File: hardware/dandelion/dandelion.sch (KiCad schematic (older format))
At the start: 102 parts, among them J1 PCB antenna, J2 USB-MICRO-B, P1 DIGITAL, P10 GIO6, P11 DCLK, P12 DIO, P13 PCB JUMPER, P14 E8A, P15 R8C PROGRAM, P16 R8C EXPAND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

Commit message: Dandelion: minor BOM correction
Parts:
- D16: Field4 (none) -> DIY
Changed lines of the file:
@@
-EESchema Schematic File Version 2  date Sat 27 Aug 2011 03:56:37 PM MDT
+EESchema Schematic File Version 2  date Sat 27 Aug 2011 04:10:09 PM MDT
 LIBS:ubertooth-symbols
 LIBS:power
@@
 F 5 "RB521S30" H 3650 9250 60  0001 C CNN "Field2"
 F 6 "DIODE SCHOTTKY 30V 200MA SOD523F" H 3650 9250 60  0001 C CNN "Field3"
+F 7 "DIY" H 3650 9250 60  0001 C CNN "Field4"
 	1    3650 9250
 	0    1    1    0

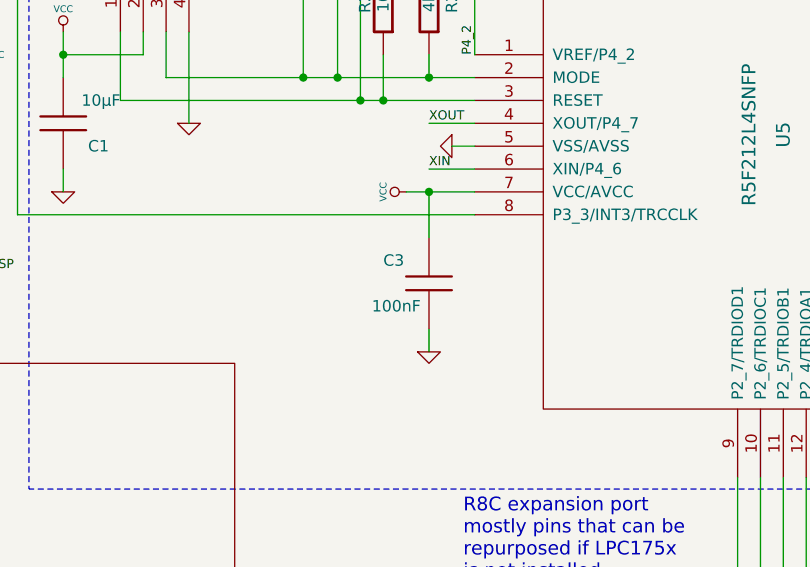
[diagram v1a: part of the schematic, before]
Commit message: Dandelion: another minor BOM correction
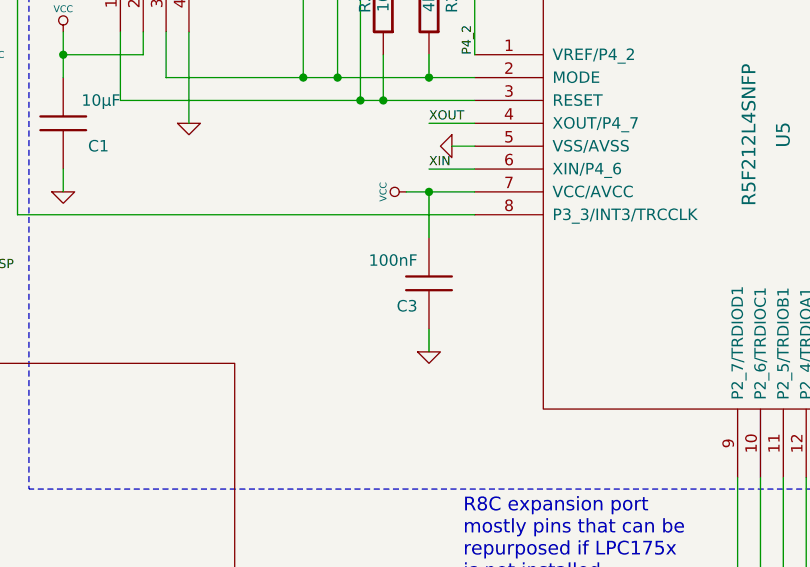
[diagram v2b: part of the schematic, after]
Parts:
- C3: footprint 0603 -> (none); Field1 TDK -> Murata; Field2 C1608X7R1H104K -> GRM155R71C104KA88D; Field3 Multilayer Ceramic Capacitors (MLCC) - SMD/SMT 0603 0.1uF 5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 -> Multilayer Ceramic Capacitors (MLCC) - SMD/SMT 0402 0.1uF 1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
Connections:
- net GND: now also C3.1; no longer C3.2
- net VCC: now also C3.2; no longer C3.1
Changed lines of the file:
@@
-EESchema Schematic File Version 2  date Sat 27 Aug 2011 04:10:09 PM MDT
+EESchema Schematic File Version 2  date Sat 27 Aug 2011 04:22:05 PM MDT
 LIBS:ubertooth-symbols
 LIBS:power
@@
 Comment4 ""
 $EndDescr
+$Comp
+L C C3
+U 1 1 4E596DF5
+P 12600 3100
+F 0 "C3" H 12650 3200 50  0000 L CNN
+F 1 "100nF" H 12650 3000 50  0000 L CNN
+F 4 "Murata" H 12600 3100 60  0001 C CNN "Field1"
+F 5 "GRM155R71C104KA88D" H 12600 3100 60  0001 C CNN "Field2"
+F 6 "Multilayer Ceramic Capacitors (MLCC) - SMD/SMT 0402 0.1uF 16volts X7R 10%" H 12600 3100 60  0001 C CNN "Field3"
+	1    12600 3100
+	-1   0    0    1
+$EndComp
 NoConn ~ 11900 1100
 Connection ~ 12300 2300
@@
 	1    0    0    -1
 $EndComp
-$Comp
-L C C3
-U 1 1 4E583A6B
-P 12600 3100
-F 0 "C3" H 12400 3200 50  0000 L CNN
-F 1 "100nF" H 12350 3000 50  0000 L CNN
-F 2 "0603" H 12600 3100 60  0001 C CNN
-F 4 "TDK" H 12600 3100 60  0001 C CNN "Field1"
-F 5 "C1608X7R1H104K" H 12600 3100 60  0001 C CNN "Field2"
-F 6 "Multilayer Ceramic Capacitors (MLCC) - SMD/SMT 0603 0.1uF 50volts X7R 10%" H 12600 3100 60  0001 C CNN "Field3"
-	1    12600 3100
-	1    0    0    -1
-$EndComp

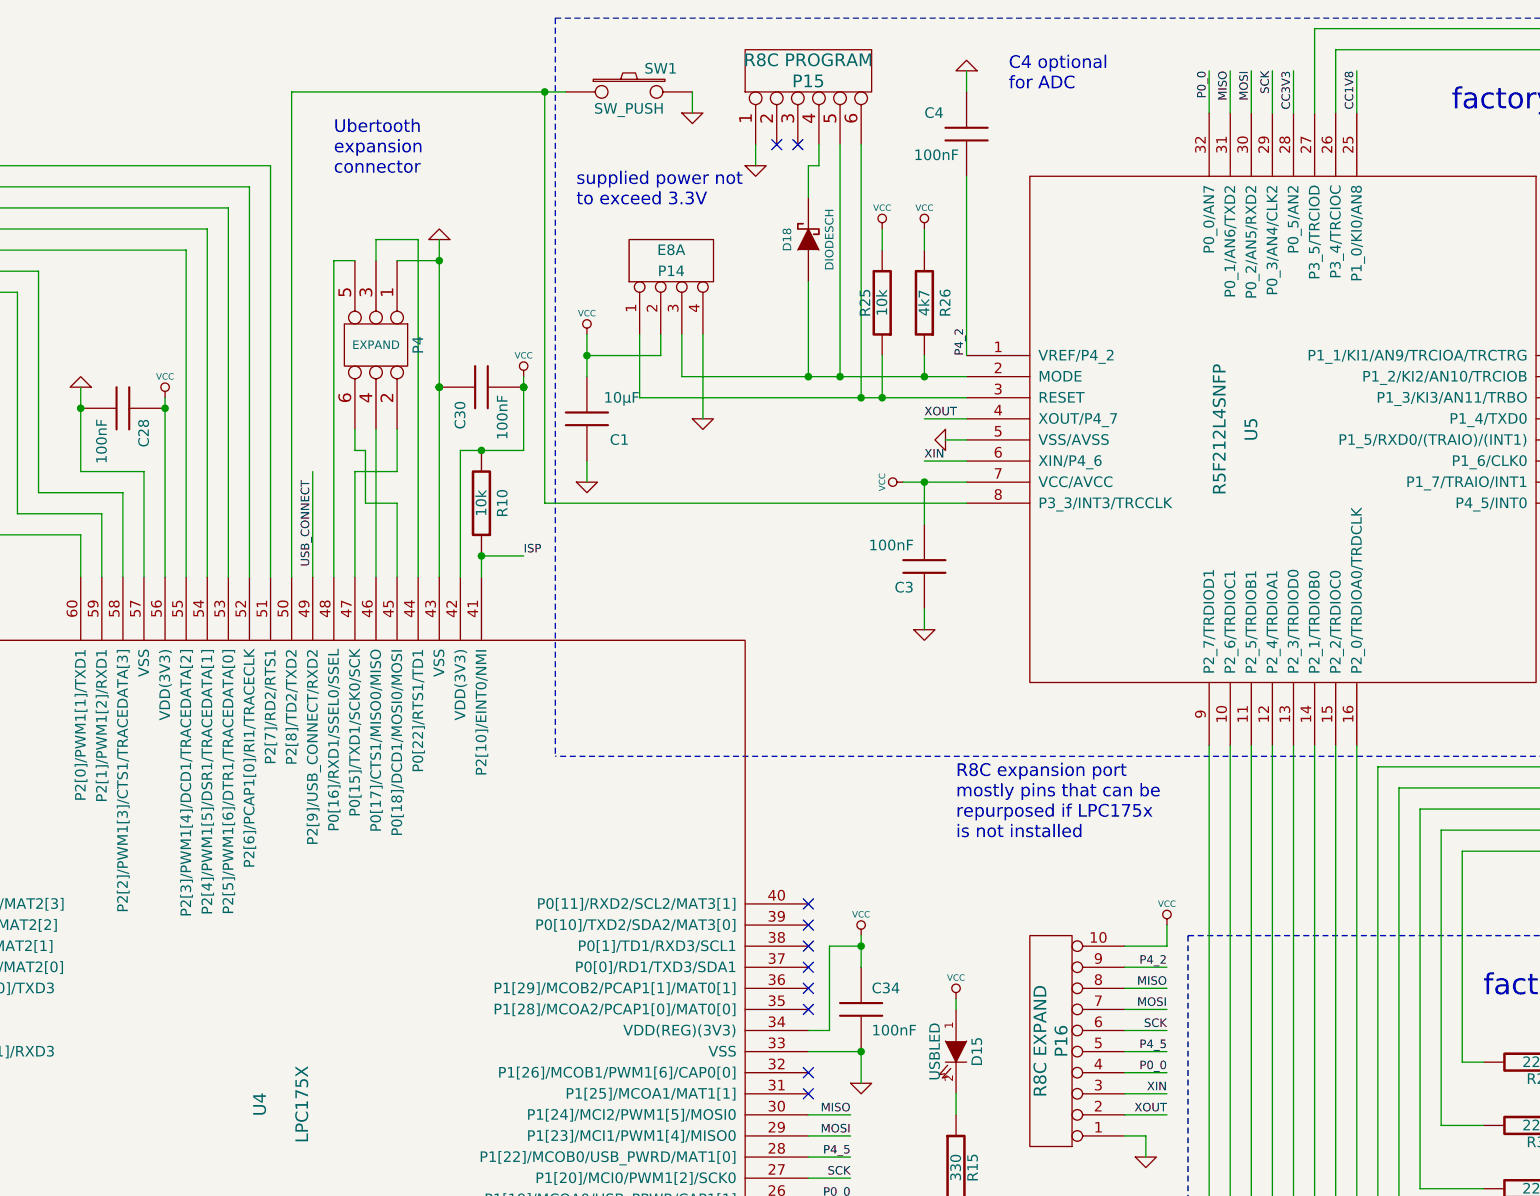
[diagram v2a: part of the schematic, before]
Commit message: Dandelion: P14/P15 notes
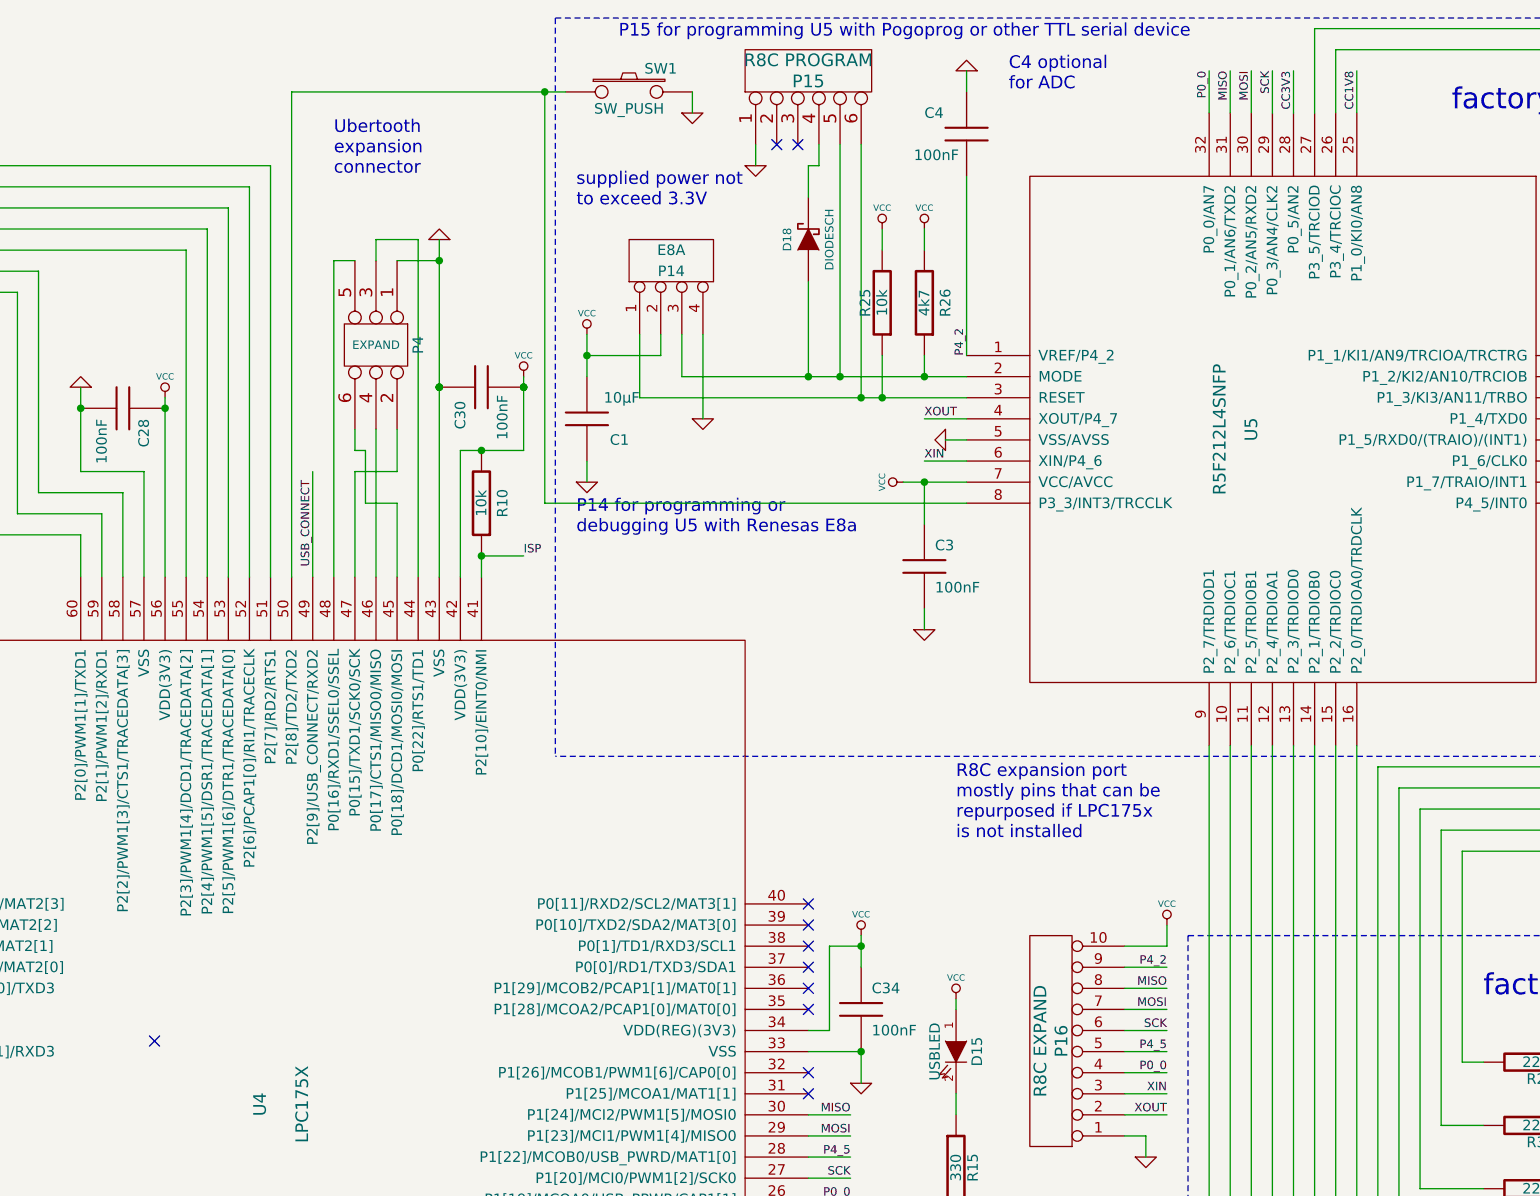
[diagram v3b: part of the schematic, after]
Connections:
- net GND: now also C3.2; no longer C3.1
- net VCC: now also C3.1; no longer C3.2
- no-connect marks 27 -> 28
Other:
- note added: "P14 for programming or\ndebugging U5 with Renesas E8a"
- note added: "P15 for programming U5 with Pogoprog or other TTL serial device"
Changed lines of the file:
@@
-EESchema Schematic File Version 2  date Sat 27 Aug 2011 04:22:05 PM MDT
+EESchema Schematic File Version 2  date Sat 27 Aug 2011 10:34:23 PM MDT
 LIBS:ubertooth-symbols
 LIBS:power
@@
 Sheet 1 1
 Title "Dandelion"
-Date "27 aug 2011"
+Date "28 aug 2011"
 Rev "$Rev$"
 Comp "Copyright 2010, 2011 Michael Ossmann"
@@
 Comment4 ""
 $EndDescr
+NoConn ~ 8950 5350
+Text Notes 11150 600  0    60   ~ 0
+P15 for programming U5 with Pogoprog or other TTL serial device
+Text Notes 10950 2950 0    60   ~ 0
+P14 for programming or\ndebugging U5 with Renesas E8a
 $Comp
 L C C3
@@
 F 6 "Multilayer Ceramic Capacitors (MLCC) - SMD/SMT 0402 0.1uF 16volts X7R 10%" H 12600 3100 60  0001 C CNN "Field3"
 	1    12600 3100
-	-1   0    0    1
+	1    0    0    -1
 $EndComp
 NoConn ~ 11900 1100

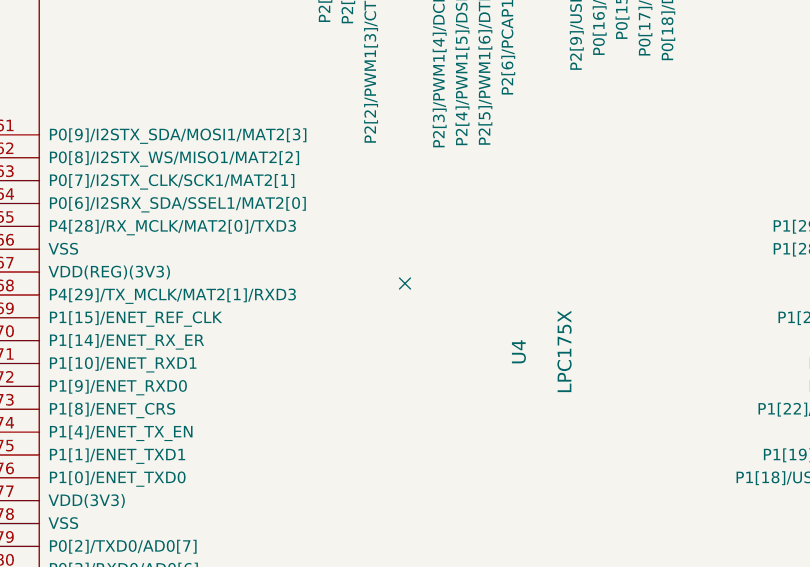
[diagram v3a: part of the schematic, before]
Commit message: Dandelion: reverted SW1 to FSM2JSMA. The actual part installed will be a Chinese component with a footprint similar to the FSM2JSMA.
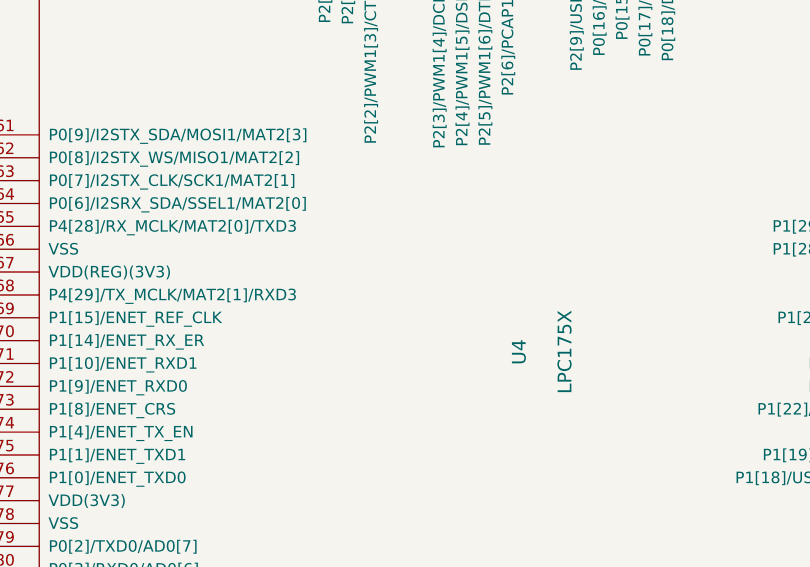
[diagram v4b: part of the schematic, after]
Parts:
- SW1: Field1 APEM Components -> TE Connectivity; Field2 ADTSM62RVTR -> FSM2JSMA; Field3 SWITCH TACT SPST 12VDC 260GF -> SWITCH TACT 6MM SMD GULL WING
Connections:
- no-connect marks 28 -> 27
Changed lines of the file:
@@
-EESchema Schematic File Version 2  date Sat 27 Aug 2011 10:34:23 PM MDT
+EESchema Schematic File Version 2  date Sat 27 Aug 2011 11:30:37 PM MDT
 LIBS:ubertooth-symbols
 LIBS:power
@@
 Comment4 ""
 $EndDescr
-NoConn ~ 8950 5350
 Text Notes 11150 600  0    60   ~ 0
 P15 for programming U5 with Pogoprog or other TTL serial device
@@
 F 0 "SW1" H 11350 960 50  0000 C CNN
 F 1 "SW_PUSH" H 11200 770 50  0000 C CNN
-F 4 "APEM Components" H 11200 850 60  0001 C CNN "Field1"
-F 5 "ADTSM62RVTR" H 11200 850 60  0001 C CNN "Field2"
-F 6 "SWITCH TACT SPST 12VDC 260GF" H 11200 850 60  0001 C CNN "Field3"
+F 4 "TE Connectivity" H 11200 850 60  0001 C CNN "Field1"
+F 5 "FSM2JSMA" H 11200 850 60  0001 C CNN "Field2"
+F 6 "SWITCH TACT 6MM SMD GULL WING" H 11200 850 60  0001 C CNN "Field3"
 	1    11200 850
 	1    0    0    -1

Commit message: Dandelion: module selection
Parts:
- C15: symbol C -> CP1
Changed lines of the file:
@@
-EESchema Schematic File Version 2  date Sat 27 Aug 2011 11:30:37 PM MDT
+EESchema Schematic File Version 2  date Sun 28 Aug 2011 11:17:45 AM MDT
 LIBS:ubertooth-symbols
 LIBS:power
@@
 $EndComp
 $Comp
-L C C15
+L CP1 C15
 U 1 1 4E5449AD
 P 4150 9850

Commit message: Dandelion: started layout, cut ATEST lines to make layout easier
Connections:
- net ATEST1: no longer names the net of P5.3, U4.7 (P0[25]/AD0[2]/I2SRX_SDA/TXD3)
- net ATEST1: no longer U3.47 (ATEST1)
- net ATEST2: no longer names the net of P5.4, U4.6 (P0[26]/AD0[3]/AOUT/RXD3)
- net ATEST2: no longer U3.46 (ATEST2)
- no-connect marks 27 -> 29
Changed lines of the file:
@@
-EESchema Schematic File Version 2  date Sun 28 Aug 2011 11:17:45 AM MDT
+EESchema Schematic File Version 2  date Sun 28 Aug 2011 12:50:07 PM MDT
 LIBS:ubertooth-symbols
 LIBS:power
@@
 Comment4 ""
 $EndDescr
+NoConn ~ 3500 1950
+NoConn ~ 3600 1950
 Text Notes 11150 600  0    60   ~ 0
 P15 for programming U5 with Pogoprog or other TTL serial device
@@
 Wire Wire Line
 	1350 6750 1450 6750
-Wire Wire Line
-	3600 1950 3600 1650
 Connection ~ 3300 7250
 Wire Wire Line
@@
 	1900 6950 2100 6950
 Connection ~ 2000 6950
-Wire Wire Line
-	3500 1950 3500 1650
 Wire Wire Line
 	1400 6550 1350 6550
@@
 Text Label 5300 2850 0    40   ~ 0
 GIO6
-Text Label 8800 9900 0    40   ~ 0
-ATEST1
-Text Label 8800 9800 0    40   ~ 0
-ATEST2
-Text Label 3600 1950 1    40   ~ 0
-ATEST2
-Text Label 3500 1950 1    40   ~ 0
-ATEST1
 $Comp
 L VCC #PWR020

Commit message: Dandelion: layout nearly complete
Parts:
- removed P5: ANALOG, symbol CONN_5
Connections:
- no-connect marks 29 -> 32
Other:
- note removed: "analog expansion port"
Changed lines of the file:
@@
-EESchema Schematic File Version 2  date Sun 28 Aug 2011 12:50:07 PM MDT
+EESchema Schematic File Version 2  date Sun 28 Aug 2011 04:47:55 PM MDT
 LIBS:ubertooth-symbols
 LIBS:power
@@
 Comment4 ""
 $EndDescr
+NoConn ~ 9100 8150
+NoConn ~ 9200 8150
+NoConn ~ 10200 8150
 NoConn ~ 3500 1950
 NoConn ~ 3600 1950
@@
 	16350 5450 16250 5450
 Wire Wire Line
-	8900 9650 8900 9700
-Wire Wire Line
-	8900 9700 8800 9700
-Wire Wire Line
-	8800 10000 10200 10000
-Wire Wire Line
-	10200 10000 10200 8150
-Wire Wire Line
-	9100 8150 9100 9800
-Wire Wire Line
-	9100 9800 8800 9800
-Wire Wire Line
 	7650 2000 7750 2000
 Wire Wire Line
@@
 Wire Wire Line
 	7750 1100 7750 1050
-Wire Wire Line
-	9200 8150 9200 9900
-Wire Wire Line
-	9200 9900 8800 9900
-Wire Wire Line
-	8900 10200 8900 10100
-Wire Wire Line
-	8900 10100 8800 10100
 Wire Wire Line
 	15750 5450 15850 5450
@@
 Text Notes 6950 800  0    60   ~ 0
 digital expansion port
-Text Notes 7650 10300 0    60   ~ 0
-analog expansion port
 $Comp
 L 1V8 #PWR018
@@
 $EndComp
 $Comp
-L VCC #PWR057
-U 1 1 4E460BA7
-P 8900 9650
-F 0 "#PWR057" H 8900 9750 30  0001 C CNN
-F 1 "VCC" H 8900 9750 30  0000 C CNN
-	1    8900 9650
-	1    0    0    -1
-$EndComp
-$Comp
-L GND #PWR058
-U 1 1 4E460B9D
-P 8900 10200
-F 0 "#PWR058" H 8900 10200 30  0001 C CNN
-F 1 "GND" H 8900 10130 30  0001 C CNN
-	1    8900 10200
-	1    0    0    -1
-$EndComp
-$Comp
-L CONN_5 P5
-U 1 1 4E460B4D
-P 8400 9900
-F 0 "P5" V 8350 9900 50  0000 C CNN
-F 1 "ANALOG" V 8450 9900 50  0000 C CNN
-F 4 "DNP" V 8400 9900 60  0001 C CNN "Field4"
-	1    8400 9900
-	-1   0    0    1
-$EndComp
-$Comp

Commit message: Dandelion: corrected 68pF value (C6,C12,C18)
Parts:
- C12, C18, C6: value 68nF -> 68pF
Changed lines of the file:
@@
-EESchema Schematic File Version 2  date Sun 28 Aug 2011 04:47:55 PM MDT
+EESchema Schematic File Version 2  date Mon 29 Aug 2011 01:13:52 AM MDT
 LIBS:ubertooth-symbols
 LIBS:power
@@
 Sheet 1 1
 Title "Dandelion"
-Date "28 aug 2011"
+Date "29 aug 2011"
 Rev "$Rev$"
 Comp "Copyright 2010, 2011 Michael Ossmann"
@@
 P 3700 5050
 F 0 "C12" H 3750 5150 50  0000 L CNN
-F 1 "68nF" H 3750 4950 50  0000 L CNN
+F 1 "68pF" H 3750 4950 50  0000 L CNN
 F 4 "Murata" H 3700 5050 60  0001 C CNN "Field1"
 F 5 "GRM1555C1H680JZ01D" H 3700 5050 60  0001 C CNN "Field2"
@@
 P 5200 1850
 F 0 "C18" H 5250 1950 50  0000 L CNN
-F 1 "68nF" H 5250 1750 50  0000 L CNN
+F 1 "68pF" H 5250 1750 50  0000 L CNN
 F 4 "Murata" H 5200 1850 60  0001 C CNN "Field1"
 F 5 "GRM1555C1H680JZ01D" H 5200 1850 60  0001 C CNN "Field2"
@@
 P 2200 1850
 F 0 "C6" H 2250 1950 50  0000 L CNN
-F 1 "68nF" H 2250 1750 50  0000 L CNN
+F 1 "68pF" H 2250 1750 50  0000 L CNN
 F 4 "Murata" H 2200 1850 60  0001 C CNN "Field1"
 F 5 "GRM1555C1H680JZ01D" H 2200 1850 60  0001 C CNN "Field2"
